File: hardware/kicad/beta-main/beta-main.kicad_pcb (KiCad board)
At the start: 4 copper layers, 77.4 x 158.9 mm, 83 parts, among them J1 AUDIO, J10 Servo Socket, J11 Servo Socket, J12 Servo Socket, J13 Servo Socket, J14 Conn_01x04_Pin, J15 Conn_01x04_Pin, J16 Conn_01x04_Pin, J17 Conn_01x04_Pin, J18 XT60, J19 FAN0, J2 USB3-0, J20 FAN1, J21 PWR, J3 USB3-1, J4 USB3-1, J5 DSI, J6 USB3_A, J7 USB3-1, J8 CSI, J9 USB3_A, Q1 MMBT3906, Q2 IRLML6246TRP, U1 MAX98357A, U2 74LVC1G126, U3 BNO086, U4 74LVC1G126, U5 AP3441SHE-7B, U6 TPS56624x, U7 AP2553W6

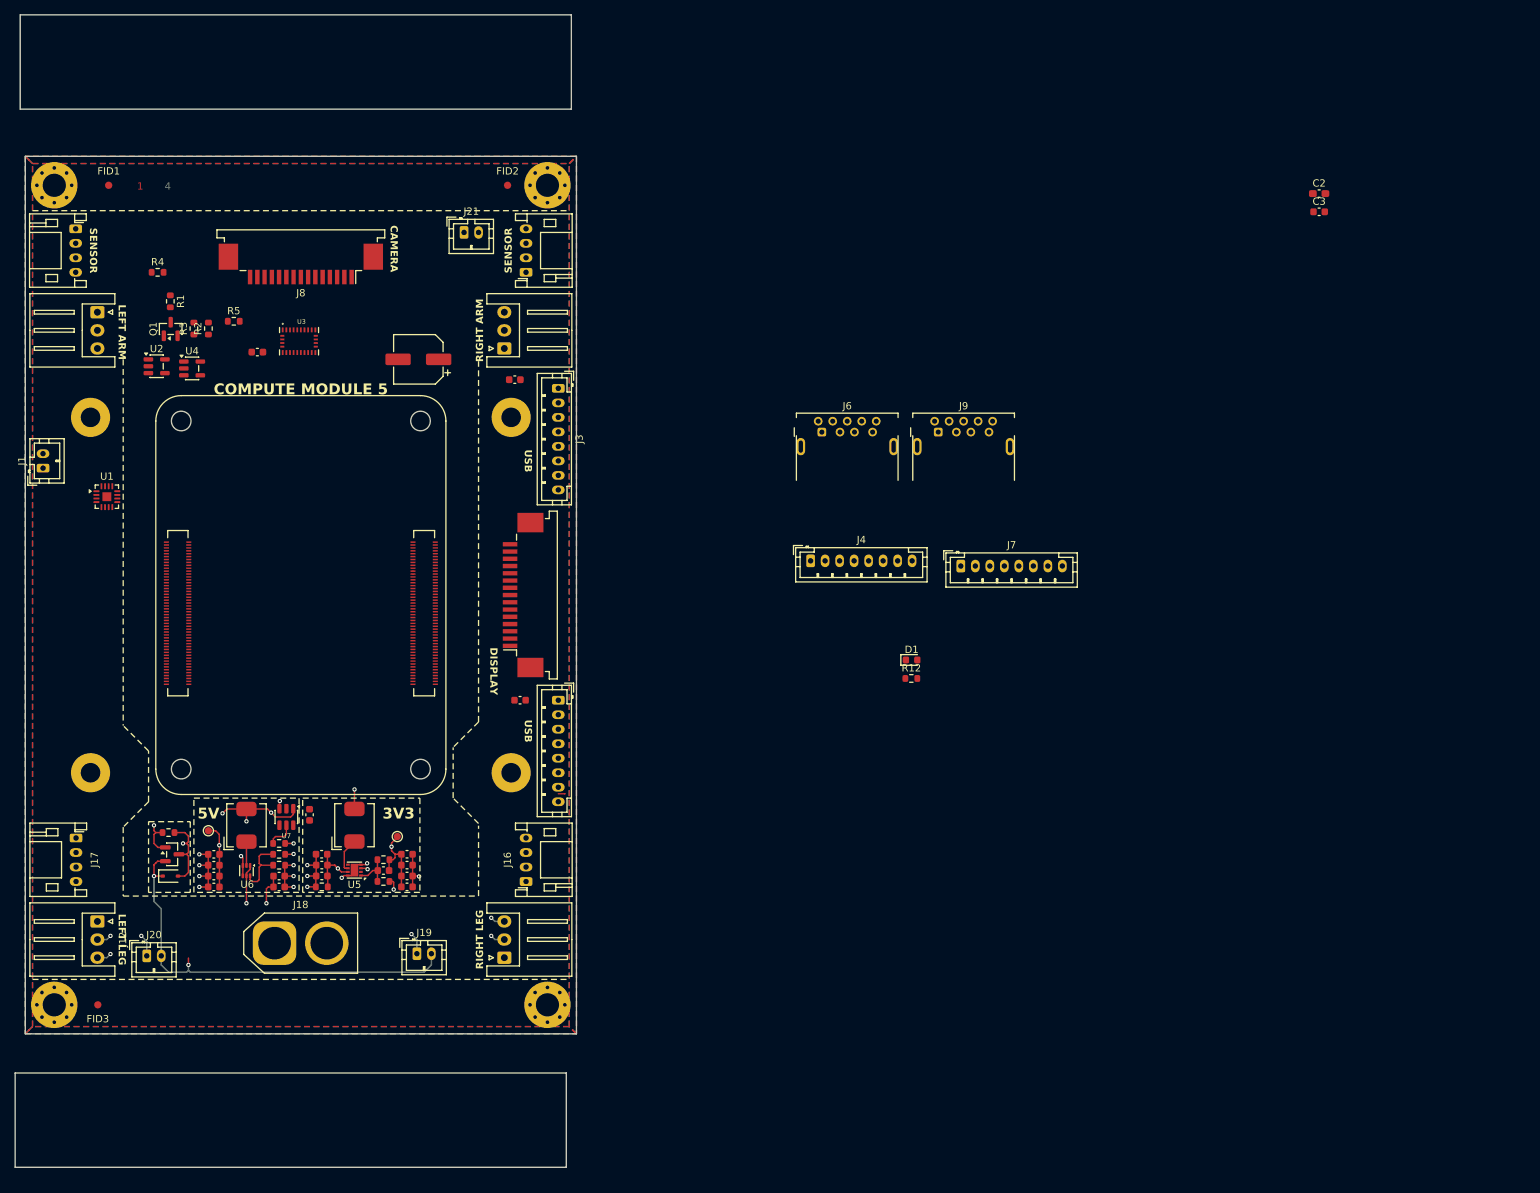
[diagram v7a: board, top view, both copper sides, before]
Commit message: route servo controller
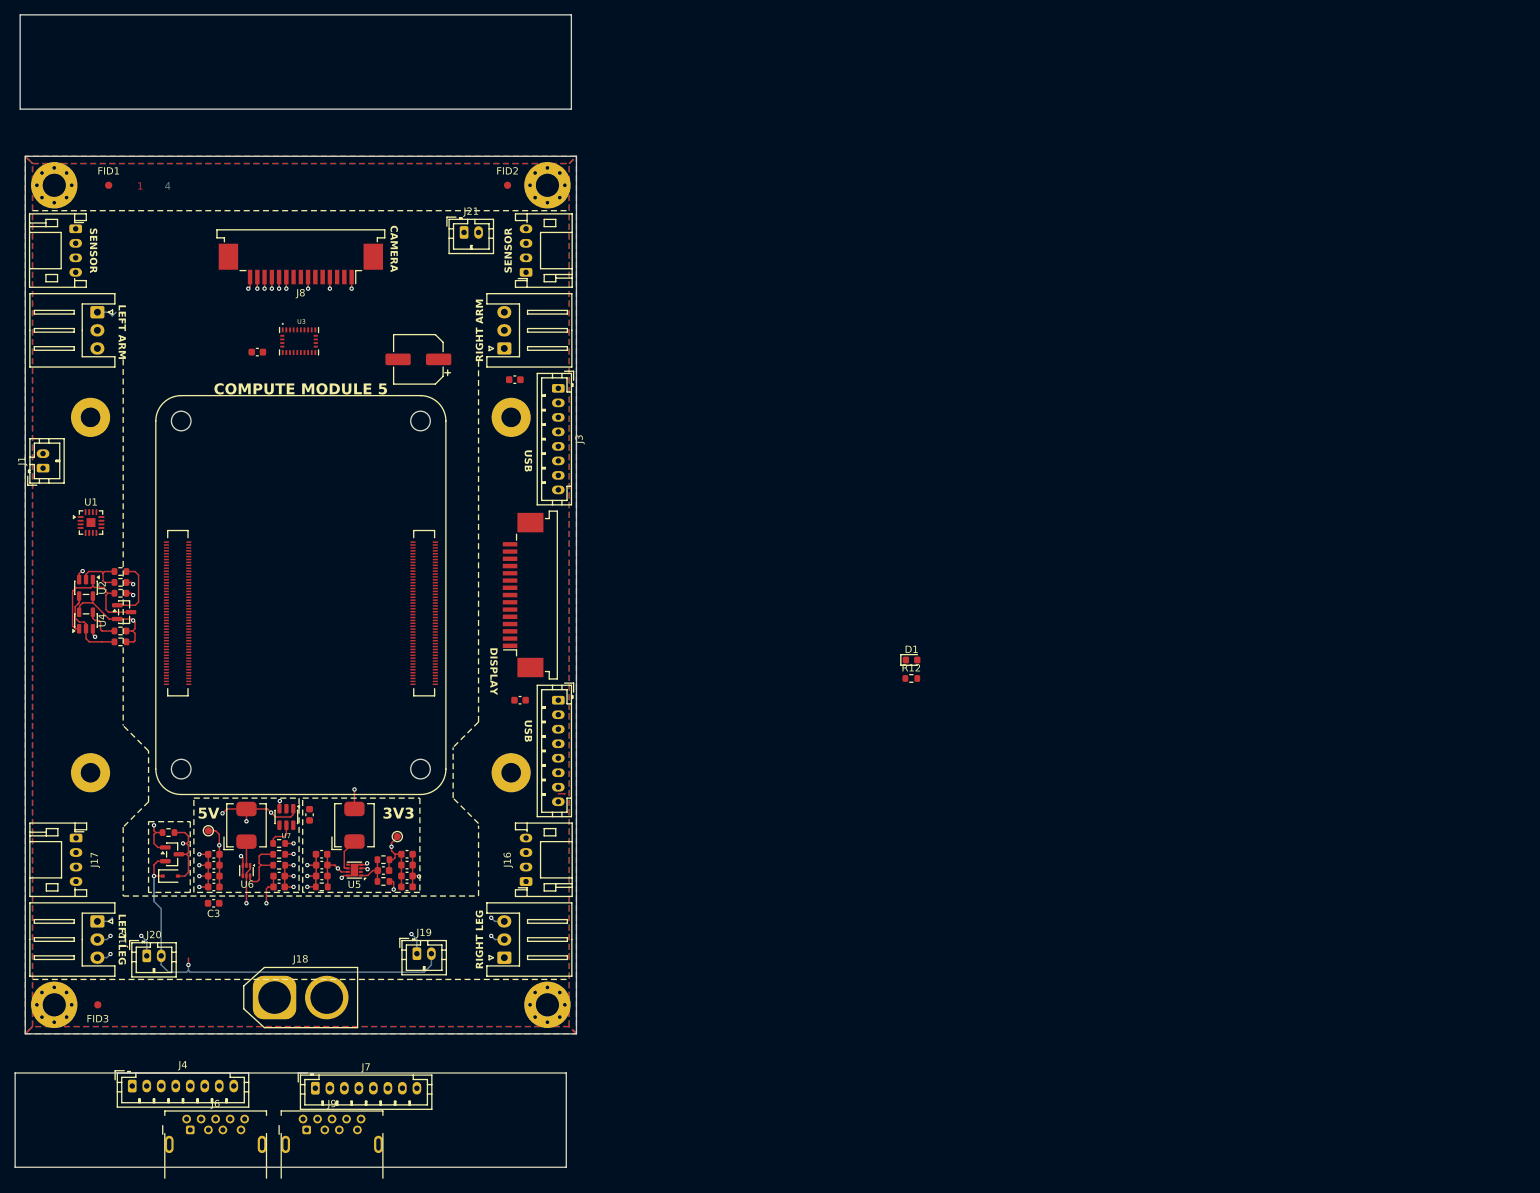
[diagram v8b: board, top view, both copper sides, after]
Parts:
- removed C2: 220u, Capacitor_SMD:C_0603_1608Metric_Pad1.08x0.95mm_HandSolder
- moved C3 179.8 mm to (88.0, 142.5), turned to 180 degrees
- moved J6 129.8 mm to (84.8, 173.8)
- moved J9 129.8 mm to (100.8, 173.8)
- moved J4 118.3 mm to (76.8, 167.7)
- moved J7 114.5 mm to (102.0, 168.0)
- moved R4 51.2 mm to (75.1, 106.5), turned to 180 degrees
- moved R5 45.5 mm to (75.1, 105.0), turned to 180 degrees
- moved R1 40.8 mm to (75.1, 99.8), turned to 180 degrees
- moved Q1 39.6 mm to (75.6, 102.4), turned to 0 degrees
- moved U4 37.7 mm to (70.4, 103.5), turned to 90 degrees
- moved R3 36.4 mm to (75.1, 98.3), turned to 180 degrees
- moved R2 35.6 mm to (75.1, 96.8), turned to 180 degrees
- moved U2 32.1 mm to (70.4, 99.0), turned to -90 degrees
- moved J18 7.50 mm to (96.4, 155.5)
- moved U1 4.18 mm to (71.1, 90.0)
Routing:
- net /Peripherals/TXEN: track 0.00 -> 19.3 mm
- net +3V3: track 13.9 -> 32.3 mm, vias 2 -> 5
- net /Peripherals/SIG: track 0.00 -> 16.4 mm
- net GND: track 54.7 -> 64.8 mm, vias 19 -> 26
- net Net-(Q1-B): track 0.00 -> 8.71 mm
- net /GPIO/UART3_TX: track 0.00 -> 7.75 mm
- net /GPIO/UART3_RX: track 0.00 -> 5.12 mm
- net /SDA1: track 0.00 -> 1.60 mm, vias 0 -> 1
- net /SCL1: track 0.00 -> 1.60 mm, vias 0 -> 1
- net /CAM_GPIO1: track 0.00 -> 1.60 mm, vias 0 -> 1
- net /CAM_GPIO0: track 0.00 -> 1.60 mm, vias 0 -> 1
